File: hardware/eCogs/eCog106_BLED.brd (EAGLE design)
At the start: 47.5 x 28 mm, 23 parts

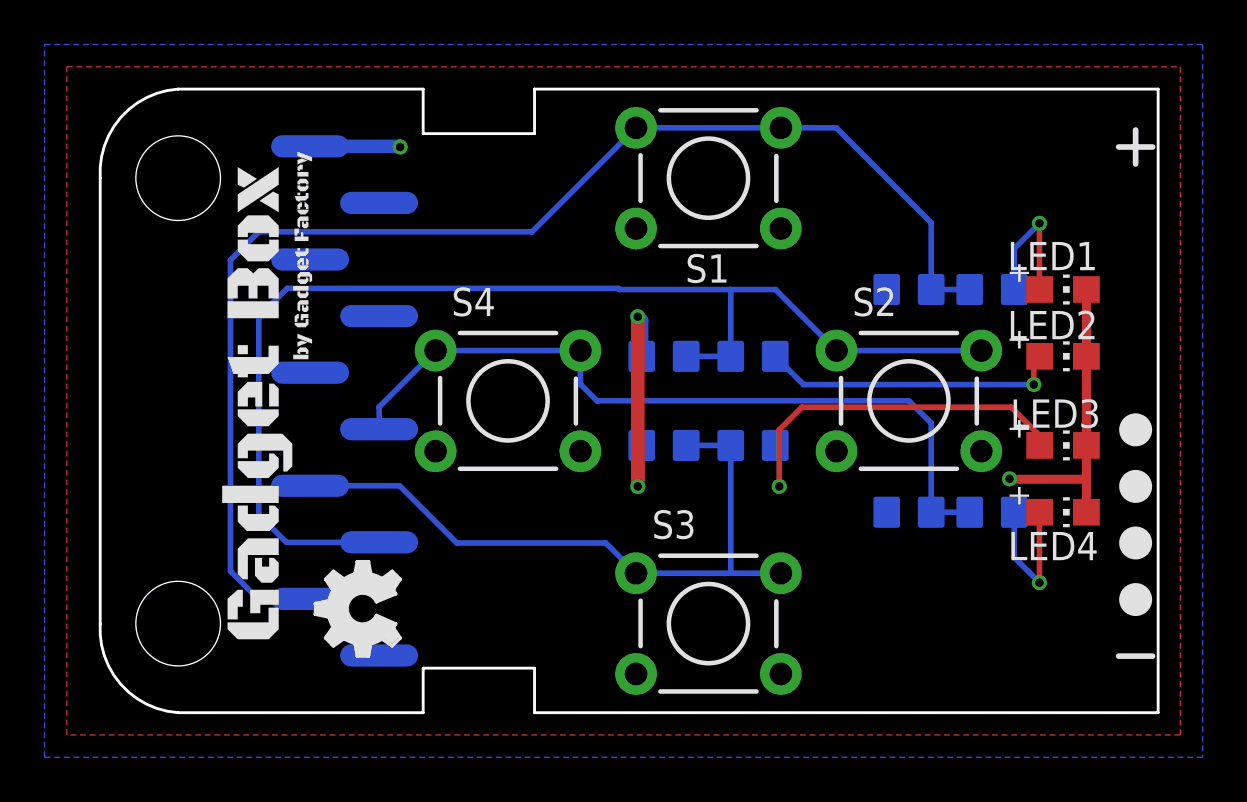
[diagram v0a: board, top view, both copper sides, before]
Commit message: Update eCogs to through hole
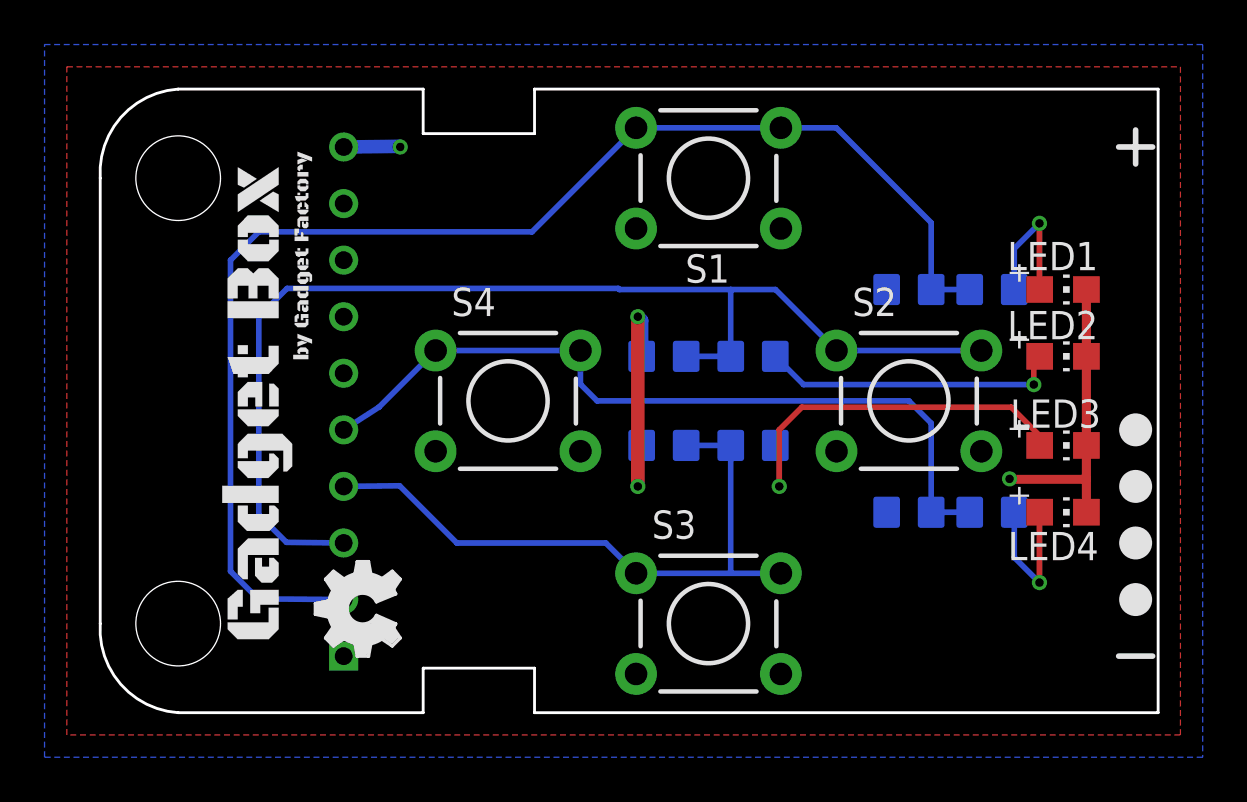
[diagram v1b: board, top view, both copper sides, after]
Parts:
- ECOG: value ECOG_GENERAL_ROWECOG_GENERAL_SMD -> ECOG_GENERAL_ROWTHROUGHOLE; device eCogs:ECOG_GENERAL_SMD -> eCogs:ECOG_GENERAL_TH
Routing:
- net 2: track 53.9 -> 52.3 mm
- net 1: track 58.5 -> 60.0 mm
- net 3V3: track 4.06 -> 2.55 mm
- net 3: track 30.5 -> 29.0 mm
- net 4: track 34.8 -> 35.7 mm
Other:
- board text added: "ecog106 v2.1"
- board text removed: "ecog106 v2.0"
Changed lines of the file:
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@@
 <plain>
 <text x="45.069" y="23.715" size="0.8128" layer="22" font="vector" rot="MR0">ecog106.GadgetFactory.net</text>
-<text x="44.512" y="2.159" size="1.016" layer="22" font="vector" rot="MR0">ecog106 v2.0</text>
+<text x="44.512" y="2.159" size="1.016" layer="22" font="vector" rot="MR0">ecog106 v2.1</text>
 <text x="44.512" y="3.429" size="1.016" layer="22" font="vector" rot="MR0">Button/LED</text>
 <text x="44.512" y="4.699" size="1.016" layer="22" font="vector" rot="MR0">eCogs</text>
@@
 </autorouter>
 <elements>
-<element name="ECOG" library="eCogs" package="ECOG_GENERAL_SMD" value="ECOG_GENERAL_ROWECOG_GENERAL_SMD" x="0" y="0" smashed="yes">
-<attribute name="DIGIKEY" value="S1013EC-10-ND" x="0" y="0" size="1.778" layer="27" display="off"/>
-</element>
+<element name="ECOG" library="eCogs" package="ECOG_GENERAL_TH" value="ECOG_GENERAL_ROWTHROUGHOLE" x="0" y="0" smashed="yes"/>
 <element name="LED1" library="adafruit" package="CHIP-LED0805" value="" x="43.73" y="19" smashed="yes" rot="R270">
 <attribute name="NAME" x="41.232" y="19.867" size="1.27" layer="25"/>
@@
 <contactref element="S4" pad="3"/>
 <contactref element="S4" pad="4"/>
-<wire x1="9.92324375" y1="25.429" x2="13.941" y2="25.429" width="0.6096" layer="16"/>
+<wire x1="11.43" y1="25.4" x2="13.941" y2="25.429" width="0.6096" layer="16"/>
 <wire x1="13.941" y1="25.429" x2="13.97" y2="25.4" width="0.6096" layer="16"/>
 <via x="13.97" y="25.4" extent="1-16" drill="0.381"/>
@@
 <wire x1="33.5494" y1="26.2606" x2="37.81" y2="22" width="0.254" layer="16"/>
 <wire x1="37.81" y1="22" x2="37.81" y2="19" width="0.254" layer="16"/>
-<wire x1="9.92324375" y1="5.1110625" x2="7.5889375" y2="5.1110625" width="0.254" layer="16"/>
+<wire x1="11.43" y1="5.08" x2="7.5889375" y2="5.1110625" width="0.254" layer="16"/>
 <wire x1="7.5889375" y1="5.1110625" x2="6.35" y2="6.35" width="0.254" layer="16"/>
 <wire x1="6.35" y1="6.35" x2="6.35" y2="20.32" width="0.254" layer="16"/>
@@
 <wire x1="28.81" y1="16" x2="28.81" y2="19" width="0.254" layer="16"/>
 <wire x1="33.5588" y1="16.2606" x2="40.0612" y2="16.2606" width="0.254" layer="16"/>
-<wire x1="13.02204375" y1="7.649" x2="8.861" y2="7.649" width="0.254" layer="16"/>
+<wire x1="11.43" y1="7.62" x2="8.861" y2="7.649" width="0.254" layer="16"/>
 <wire x1="8.861" y1="7.649" x2="7.62" y2="8.89" width="0.254" layer="16"/>
 <wire x1="7.62" y1="8.89" x2="7.62" y2="17.78" width="0.254" layer="16"/>
@@
 <wire x1="28.81" y1="6.2606" x2="24.5588" y2="6.2606" width="0.254" layer="16"/>
 <wire x1="28.81" y1="12" x2="28.81" y2="6.2606" width="0.254" layer="16"/>
-<wire x1="9.92324375" y1="10.189" x2="13.941" y2="10.189" width="0.254" layer="16"/>
+<wire x1="11.43" y1="10.16" x2="13.941" y2="10.189" width="0.254" layer="16"/>
 <wire x1="13.941" y1="10.189" x2="16.51" y2="7.62" width="0.254" layer="16"/>
 <wire x1="16.51" y1="7.62" x2="23.1994" y2="7.62" width="0.254" layer="16"/>
@@
 <wire x1="36.81" y1="14" x2="37.81" y2="13" width="0.254" layer="16"/>
 <wire x1="37.81" y1="13" x2="37.81" y2="9" width="0.254" layer="16"/>
-<wire x1="13.02204375" y1="12.729" x2="13.02204375" y2="13.72384375" width="0.254" layer="16"/>
+<wire x1="11.43" y1="12.7" x2="13.02204375" y2="13.72384375" width="0.254" layer="16"/>
 <wire x1="13.02204375" y1="13.72384375" x2="15.5588" y2="16.2606" width="0.254" layer="16"/>
 </signal>
